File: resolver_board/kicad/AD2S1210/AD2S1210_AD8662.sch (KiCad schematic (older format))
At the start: 74 parts, among them IC1 AD8662, K1 JP_1, K2 V_control, K3 Power, P1 conn_stm32f4, P2 AOUT, P3 conn_motor_control, P4 JP_2, P5 JP_3, Q1 RECOM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

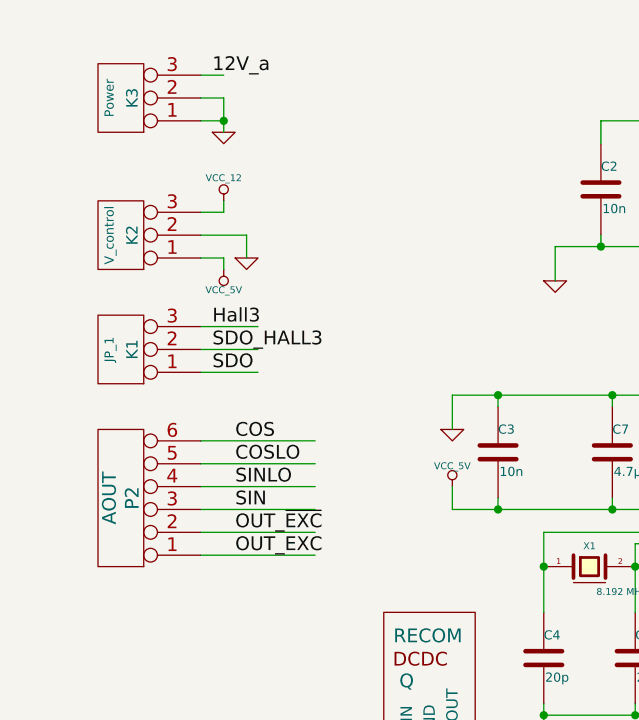
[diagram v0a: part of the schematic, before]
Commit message: voltage divider added to the resolver_board
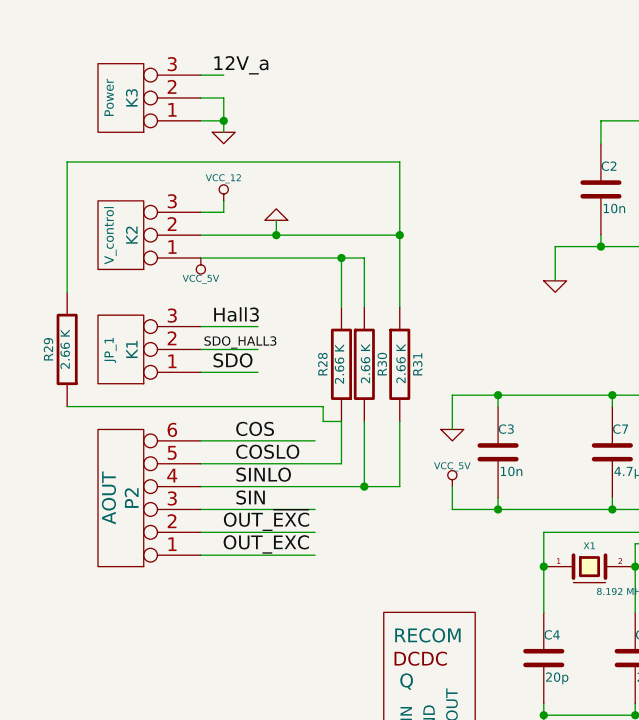
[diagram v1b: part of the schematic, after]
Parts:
- added R28, R29, R30, R31: 2.66 K, ~, symbol R
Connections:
- wire segments 352 -> 362
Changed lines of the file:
@@
 Sheet 1 1
 Title "AD2S1210"
-Date "13 mar 2015"
+Date "23 apr 2015"
 Rev "V1.2"
 Comp "P. Koenig"
@@
 Text Label 1350 5550 0    60   ~ 0
 SIN
-Text Label 1350 5650 0    60   ~ 0
+Text Label 1296 5647 0    60   ~ 0
 OUT_~EXC
-Text Label 1350 5750 0    60   ~ 0
+Text Label 1295 5746 0    60   ~ 0
 OUT_EXC
 $Comp
@@
 L VCC_5V #PWR04
 U 1 1 5360753E
-P 1300 4500
-F 0 "#PWR04" H 1300 4590 20  0001 C CNN
-F 1 "VCC_5V" H 1300 4590 30  0000 C CNN
-F 2 "" H 1300 4500 60  0000 C CNN
-F 3 "" H 1300 4500 60  0000 C CNN
-	1    1300 4500
+P 1200 4450
+F 0 "#PWR04" H 1200 4540 20  0001 C CNN
+F 1 "VCC_5V" H 1200 4540 30  0000 C CNN
+F 2 "" H 1200 4450 60  0000 C CNN
+F 3 "" H 1200 4450 60  0000 C CNN
+	1    1200 4450
 	-1   0    0    1
 $EndComp
@@
 $EndComp
 $Comp
-L GND #PWR027
-U 1 1 538D2D0C
-P 1400 4450
-F 0 "#PWR027" H 1400 4450 30  0001 C CNN
-F 1 "GND" H 1400 4380 30  0001 C CNN
-F 2 "" H 1400 4450 60  0000 C CNN
-F 3 "" H 1400 4450 60  0000 C CNN
-	1    1400 4450
-	1    0    0    -1
-$EndComp
-$Comp
 L VCC_12 #PWR028
 U 1 1 538D3331
@@
 	1    10850 4950
 	1    0    0    -1
-$EndComp
-$Comp
-L CONN_3 K2
-U 1 1 538D3FA9
-P 850 4350
-F 0 "K2" V 800 4350 50  0000 C CNN
-F 1 "V_control" V 900 4350 40  0000 C CNN
-F 2 "" H 850 4350 60  0000 C CNN
-F 3 "" H 850 4350 60  0000 C CNN
-	1    850  4350
-	-1   0    0    1
 $EndComp
 $Comp
@@
 Text Label 1250 4950 0    60   ~ 0
 SDO
-Text Label 1250 4850 0    60   ~ 0
+Text Label 1212 4850 0    40   ~ 0
 SDO_HALL3
 $Comp
@@
 	1    0    0    -1
 $EndComp
+$Comp
+L CONN_1 Drill1
+U 1 1 53ACDF41
+P 5950 7350
+F 0 "Drill1" H 6030 7350 40  0000 L CNN
+F 1 "Drill1" H 5950 7405 30  0001 C CNN
+F 2 "" H 5950 7350 60  0000 C CNN
+F 3 "" H 5950 7350 60  0000 C CNN
+	1    5950 7350
+	1    0    0    -1
+$EndComp
+$Comp
+L CONN_1 Drill2
+U 1 1 53ACDF4E
+P 5950 7450
+F 0 "Drill2" H 6030 7450 40  0000 L CNN
+F 1 "Drill2" H 5950 7505 30  0001 C CNN
+F 2 "" H 5950 7450 60  0000 C CNN
+F 3 "" H 5950 7450 60  0000 C CNN
+	1    5950 7450
+	1    0    0    -1
+$EndComp
+$Comp
+L CONN_1 Drill3
+U 1 1 53ACDF54
+P 5950 7550
+F 0 "Drill3" H 6030 7550 40  0000 L CNN
+F 1 "Drill3" H 5950 7605 30  0001 C CNN
+F 2 "" H 5950 7550 60  0000 C CNN
+F 3 "" H 5950 7550 60  0000 C CNN
+	1    5950 7550
+	1    0    0    -1
+$EndComp
+$Comp
+L CONN_1 Drill4
+U 1 1 53ACDF5A
+P 5950 7650
+F 0 "Drill4" H 6030 7650 40  0000 L CNN
+F 1 "Drill4" H 5950 7705 30  0001 C CNN
+F 2 "" H 5950 7650 60  0000 C CNN
+F 3 "" H 5950 7650 60  0000 C CNN
+	1    5950 7650
+	1    0    0    -1
+$EndComp
+$Comp
+L R R28
+U 1 1 5538BA7D
+P 1815 4915
+F 0 "R28" V 1895 4915 40  0000 C CNN
+F 1 "2.66 K" V 1822 4916 40  0000 C CNN
+F 2 "~" V 1745 4915 30  0000 C CNN
+F 3 "~" H 1815 4915 30  0000 C CNN
+	1    1815 4915
+	-1   0    0    1
+$EndComp
+$Comp
+L R R30
+U 1 1 5538BA93
+P 1915 4915
+F 0 "R30" V 1995 4915 40  0000 C CNN
+F 1 "2.66 K" V 1922 4916 40  0000 C CNN
+F 2 "~" V 1845 4915 30  0000 C CNN
+F 3 "~" H 1915 4915 30  0000 C CNN
+	1    1915 4915
+	1    0    0    -1
+$EndComp
+$Comp
+L R R31
+U 1 1 5538DCD2
+P 2070 4915
+F 0 "R31" V 2150 4915 40  0000 C CNN
+F 1 "2.66 K" V 2077 4916 40  0000 C CNN
+F 2 "~" V 2000 4915 30  0000 C CNN
+F 3 "~" H 2070 4915 30  0000 C CNN
+	1    2070 4915
+	1    0    0    -1
+$EndComp
+$Comp
+L R R29
+U 1 1 5538E206
+P 615 4850
+F 0 "R29" V 695 4850 40  0000 C CNN
+F 1 "2.66 K" V 622 4851 40  0000 C CNN
+F 2 "~" V 545 4850 30  0000 C CNN
+F 3 "~" H 615 4850 30  0000 C CNN
+	1    615  4850
+	-1   0    0    1
+$EndComp
+$Comp
+L GND #PWR?
+U 1 1 5538CAAE
+P 1530 4285
+F 0 "#PWR?" H 1530 4285 30  0001 C CNN
+F 1 "GND" H 1530 4215 30  0001 C CNN
+F 2 "" H 1530 4285 60  0000 C CNN
+F 3 "" H 1530 4285 60  0000 C CNN
+	1    1530 4285
+	-1   0    0    1
+$EndComp
+$Comp
+L CONN_3 K2
+U 1 1 538D3FA9
+P 850 4350
+F 0 "K2" V 800 4350 50  0000 C CNN
+F 1 "V_control" V 900 4350 40  0000 C CNN
+F 2 "" H 850 4350 60  0000 C CNN
+F 3 "" H 850 4350 60  0000 C CNN
+	1    850  4350
+	-1   0    0    1
+$EndComp
 Connection ~ 7900 4650
 Wire Wire Line
@@
 	1200 5550 1700 5550
 Wire Wire Line
-	1200 5450 1700 5450
-Wire Wire Line
-	1200 5350 1700 5350
+	1200 5450 2070 5450
+Wire Wire Line
+	1200 5350 1815 5350
 Wire Wire Line
 	1200 5250 1700 5250
@@
 	1300 4250 1300 4200
 Wire Wire Line
-	1400 4350 1400 4450
-Wire Wire Line
 	4000 3200 4500 3200
 Wire Wire Line
@@
 Connection ~ 5300 3200
 Connection ~ 9350 4300
-Wire Wire Line
-	1400 4350 1200 4350
-Wire Wire Line
-	1200 4450 1300 4450
-Wire Wire Line
-	1300 4450 1300 4500
 Connection ~ 1250 7400
-$Comp
-L CONN_1 Drill1
-U 1 1 53ACDF41
-P 5950 7350
-F 0 "Drill1" H 6030 7350 40  0000 L CNN
-F 1 "Drill1" H 5950 7405 30  0001 C CNN
-F 2 "" H 5950 7350 60  0000 C CNN
-F 3 "" H 5950 7350 60  0000 C CNN
-	1    5950 7350
-	1    0    0    -1
-$EndComp
-$Comp
-L CONN_1 Drill2
-U 1 1 53ACDF4E
-P 5950 7450
-F 0 "Drill2" H 6030 7450 40  0000 L CNN
-F 1 "Drill2" H 5950 7505 30  0001 C CNN
-F 2 "" H 5950 7450 60  0000 C CNN
-F 3 "" H 5950 7450 60  0000 C CNN
-	1    5950 7450
-	1    0    0    -1
-$EndComp
-$Comp
-L CONN_1 Drill3
-U 1 1 53ACDF54
-P 5950 7550
-F 0 "Drill3" H 6030 7550 40  0000 L CNN
-F 1 "Drill3" H 5950 7605 30  0001 C CNN
-F 2 "" H 5950 7550 60  0000 C CNN
-F 3 "" H 5950 7550 60  0000 C CNN
-	1    5950 7550
-	1    0    0    -1
-$EndComp
-$Comp
-L CONN_1 Drill4
-U 1 1 53ACDF5A
-P 5950 7650
-F 0 "Drill4" H 6030 7650 40  0000 L CNN
-F 1 "Drill4" H 5950 7705 30  0001 C CNN
-F 2 "" H 5950 7650 60  0000 C CNN
-F 3 "" H 5950 7650 60  0000 C CNN
-	1    5950 7650
-	1    0    0    -1
-$EndComp
+Wire Wire Line
+	615  4600 615  4030
+Wire Wire Line
+	615  4030 2070 4030
+Wire Wire Line
+	2070 4030 2070 4665
+Wire Wire Line
+	1200 4450 1915 4450
+Wire Wire Line
+	1815 4450 1815 4665
+Wire Wire Line
+	1915 4450 1915 4665
+Connection ~ 1815 4450
+Wire Wire Line
+	1200 4350 2070 4350
+Wire Wire Line
+	1530 4350 1530 4285
+Connection ~ 2070 4350
+Connection ~ 1530 4350
+Wire Wire Line
+	1815 5350 1815 5165
+Wire Wire Line
+	615  5100 1735 5100
+Wire Wire Line
+	1735 5100 1735 5165
+Wire Wire Line
+	1735 5165 1815 5165
+Wire Wire Line
+	1915 5450 1915 5165
+Wire Wire Line
+	2070 5450 2070 5165
+Connection ~ 1915 5450
 $EndSCHEMATC
